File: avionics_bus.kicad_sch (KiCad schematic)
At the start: 12 parts

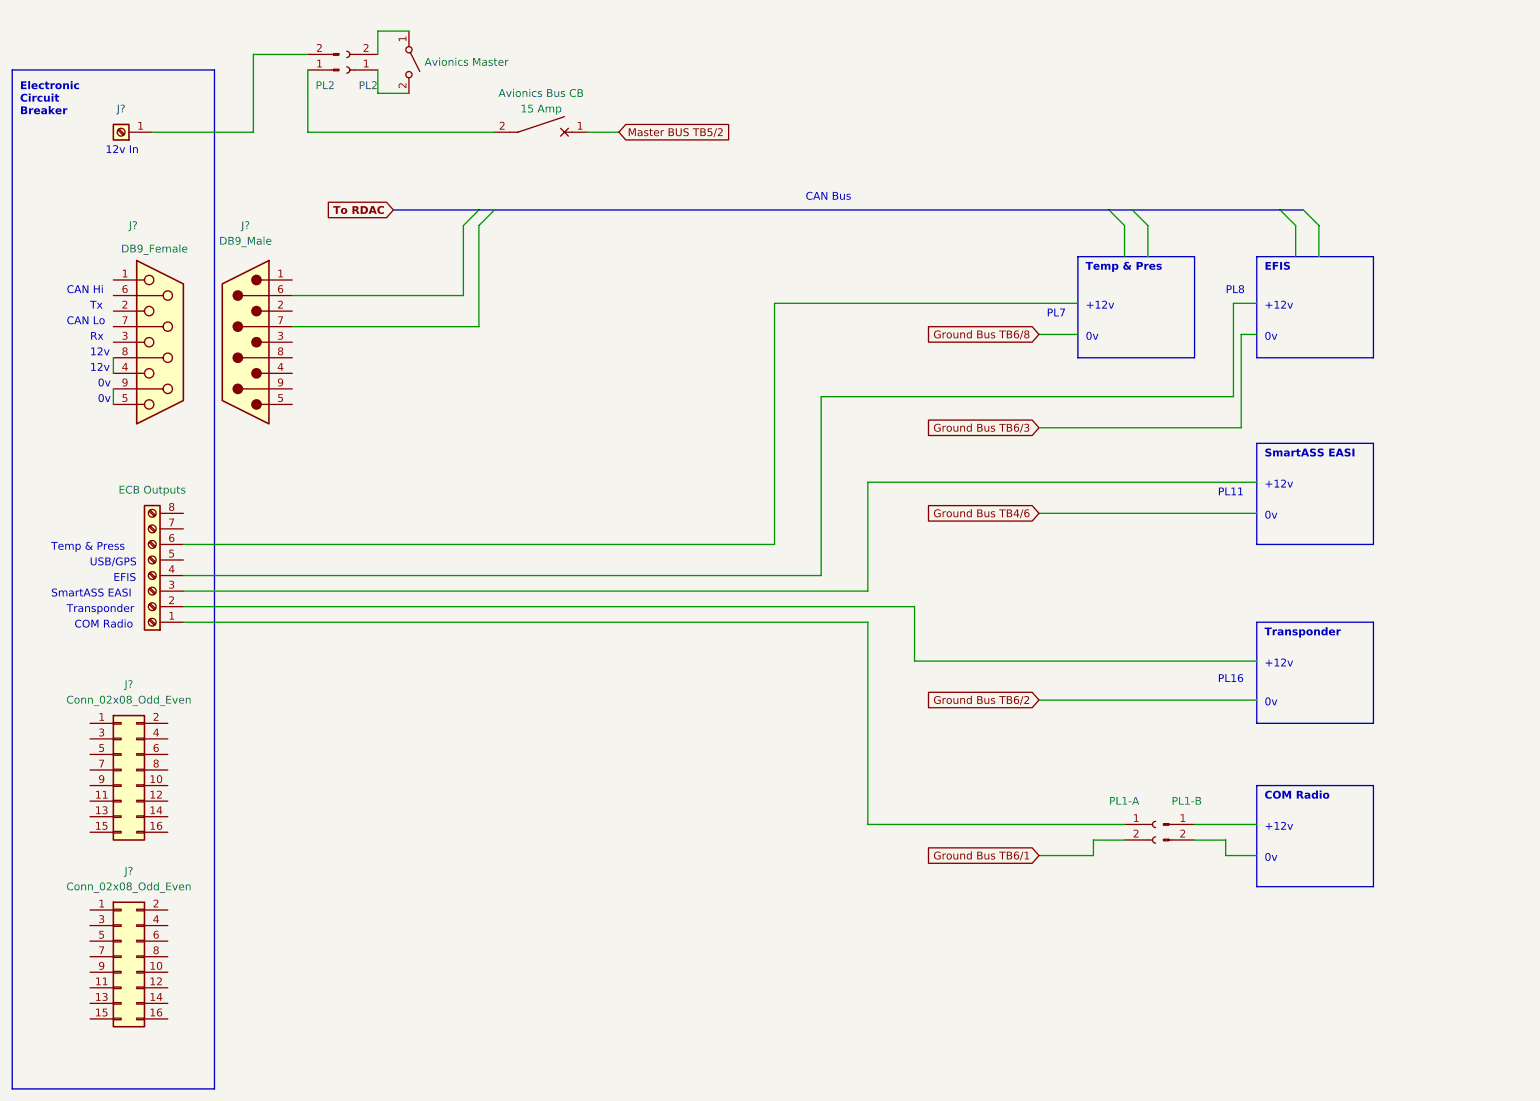
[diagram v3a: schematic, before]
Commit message: Updates from manual validation
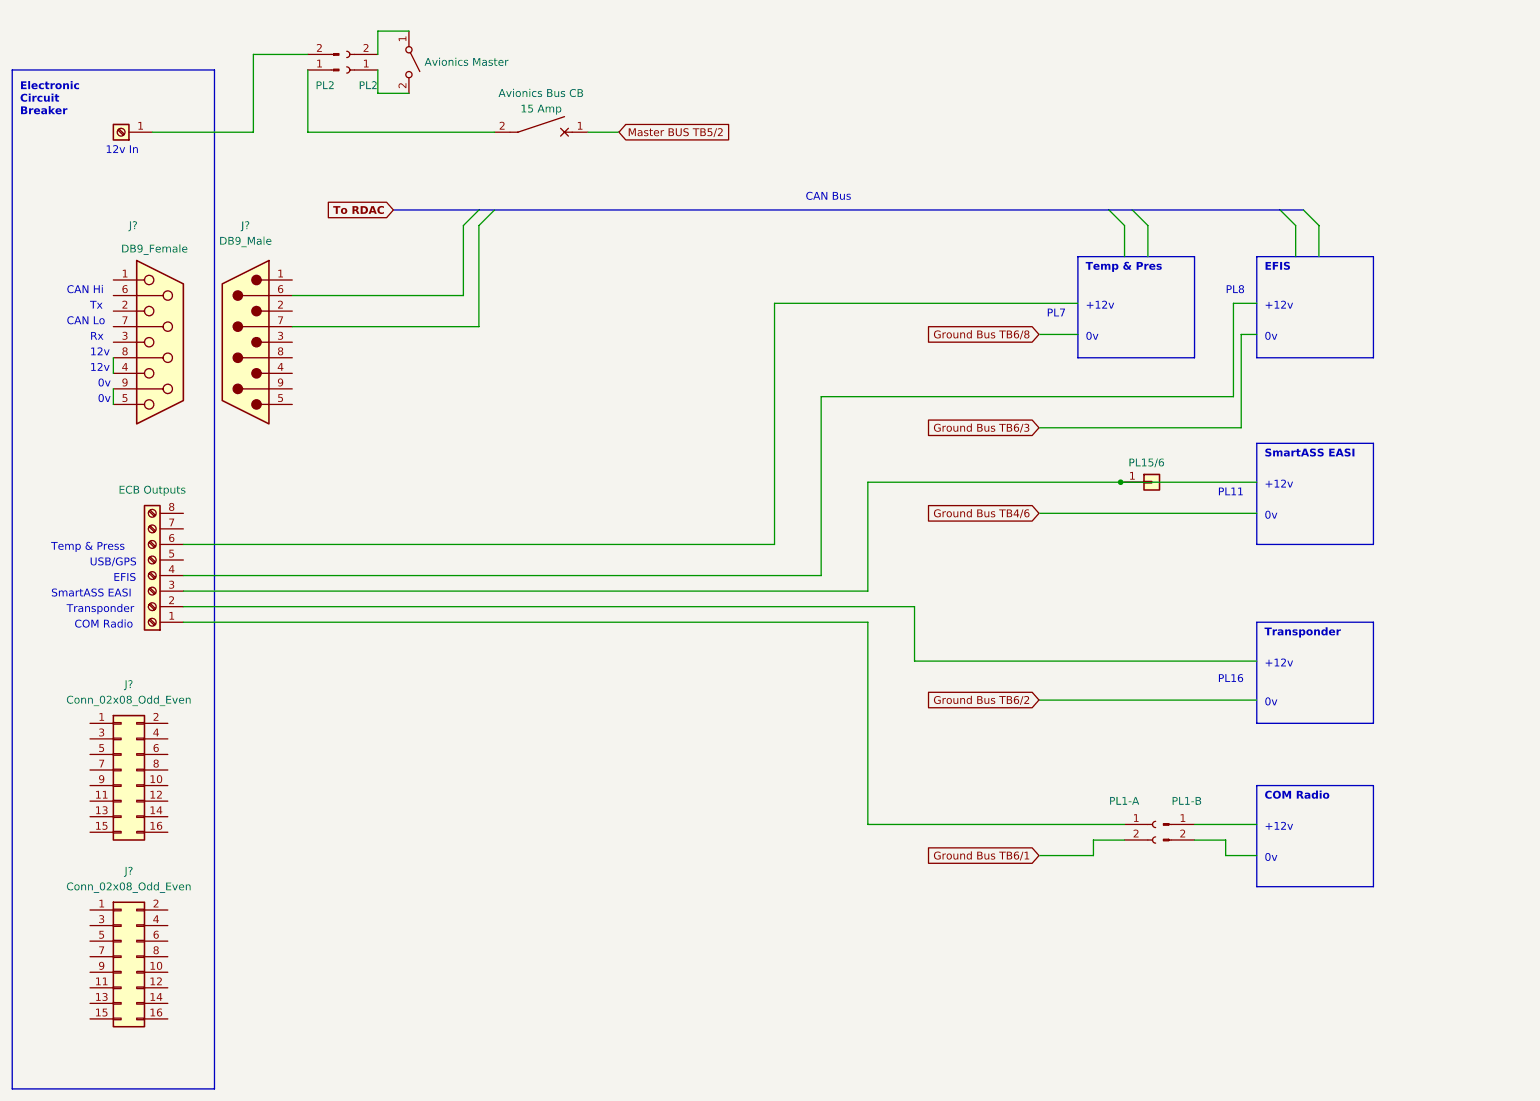
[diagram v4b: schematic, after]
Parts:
- added PL15/6: Conn_01x01, symbol Connector_Generic:Conn_01x01
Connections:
- net at J?.3 (Pin_3): now also PL15/6.1 (Pin_1)
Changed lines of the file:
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@@
   (title_block
     (title "Europa Avionics Bus")
-    (date "2022-12-19")
-    (rev "1")
+    (date "2022-12-24")
+    (rev "2")
+  )
+  (junction (at 213.995 91.44) (diameter 0) (color 0 0 0 0)
   )
   (bus_entry (at 106.68 49.53) (size 2.54 -2.54)
@@
     (stroke (width 0) (type default) (color 0 0 0 0))
   )
-  (wire (pts (xy 172.72 91.44) (xy 236.22 91.44))
+  (wire (pts (xy 172.72 91.44) (xy 213.995 91.44))
     (stroke (width 0) (type default) (color 0 0 0 0))
   )
@@
   )
   (wire (pts (xy 226.06 149.86) (xy 231.14 149.86))
+    (stroke (width 0) (type default) (color 0 0 0 0))
+  )
+  (wire (pts (xy 213.995 91.44) (xy 236.22 91.44))
     (stroke (width 0) (type default) (color 0 0 0 0))
   )
@@
     (pin "1")
     (pin "2")
+  )
+  (symbol (lib_id "Connector_Generic:Conn_01x01") (at 219.075 91.44 0) (unit 1)
+    (in_bom yes) (on_board yes)
+    (property "Reference" "PL15/6" (id 0) (at 215.265 88.265 0)
+      (effects (font (size 1.27 1.27)) (justify left))
+    )
+    (property "Value" "Conn_01x01" (id 1) (at 222.25 92.7099 0)
+      (effects (font (size 1.27 1.27)) (justify left) hide)
+    )
+    (property "Footprint" "" (id 2) (at 219.075 91.44 0)
+      (effects (font (size 1.27 1.27)) hide)
+    )
+    (property "Datasheet" "~" (id 3) (at 219.075 91.44 0)
+      (effects (font (size 1.27 1.27)) hide)
+    )
+    (pin "1")
   )
   (symbol (lib_id "Connector:Conn_01x02_Female") (at 87.63 24.13 180) (unit 1)
@@
   (symbol (lib_id "Connector:Screw_Terminal_01x01") (at 50.8 34.29 180) (unit 1)
     (in_bom yes) (on_board yes) (fields_autoplaced)
-    (property "Reference" "J?" (id 0) (at 50.8 30.48 0))
+    (property "Reference" "J?" (id 0) (at 50.8 30.48 0)
+      (effects (font (size 1.27 1.27)) hide)
+    )
     (property "Value" "Screw_Terminal_01x01" (id 1) (at 50.8 30.48 0)
       (effects (font (size 1.27 1.27)) hide)

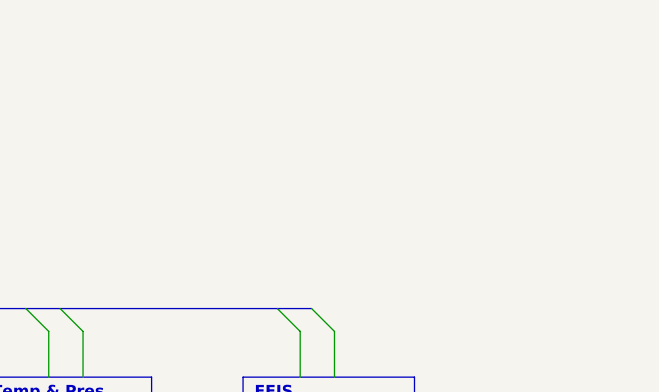
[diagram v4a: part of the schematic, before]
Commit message: Small updates to multiple sheets, and major update to SmartAss sheet
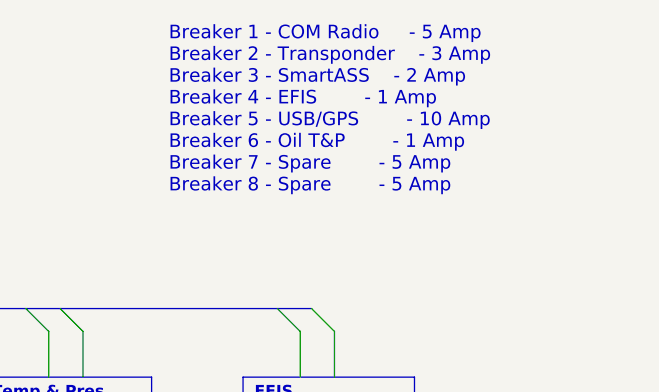
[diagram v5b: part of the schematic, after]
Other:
- note added: "Breaker 1 - COM Radio - 5 Amp Breaker 2 - Transponder - 3 Amp Breaker 3 - SmartASS - 2 Amp Breaker 4 - EFIS - 1 Amp Breaker 5 - USB/GPS - 10 Amp Breaker 6 - Oil T&P - 1 Amp Breaker 7 - Spare - 5 Amp Breaker 8 - Spare - 5 Amp"
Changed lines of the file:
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@@
   (title_block
     (title "Europa Avionics Bus")
-    (date "2022-12-24")
-    (rev "2")
+    (date "2022-12-29")
+    (rev "3")
   )
   (junction (at 213.995 91.44) (diameter 0) (color 0 0 0 0)
@@
     (effects (font (size 1.27 1.27) bold) (justify left bottom))
   )
+  (text "Breaker 1 - COM Radio 	- 5 Amp\nBreaker 2 - Transponder	- 3 Amp\nBreaker 3 - SmartASS	- 2 Amp\nBreaker 4 - EFIS		- 1 Amp\nBreaker 5 - USB/GPS		- 10 Amp\nBreaker 6 - Oil T&P		- 1 Amp\nBreaker 7 - Spare		- 5 Amp\nBreaker 8 - Spare		- 5 Amp"
+    (at 227.965 34.29 0)
+    (effects (font (size 1.5 1.5)) (justify left bottom))
+  )
   (text "USB/GPS" (at 53.34 105.41 180)
